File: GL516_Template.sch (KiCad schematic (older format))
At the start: 259 parts, among them J1 Conn_01x02, J10 Conn_01x01, J11 Conn_01x01, J12 Conn_01x01, J13 Conn_01x01, J14 Conn_01x01, J15 Conn_01x01, J16 Conn_01x01, J17 Conn_01x01, J2 Conn_01x01, J3 Conn_01x01, J4 Conn_01x01, J5 Conn_01x01, J6 Conn_01x01, J7 Conn_01x01, J8 Conn_01x01, J9 Conn_01x01, SW1 SW_PUSH, SW10 SW_PUSH, SW11 SW_PUSH, SW12 SW_PUSH, SW13 SW_PUSH, SW14 SW_PUSH, SW15 SW_PUSH, SW16 SW_PUSH, SW17 SW_PUSH, SW18 SW_PUSH, SW19 SW_PUSH, SW2 SW_PUSH, SW20 SW_PUSH, SW21 SW_PUSH, SW22 SW_PUSH, SW23 SW_PUSH, SW24 SW_PUSH, SW25 SW_PUSH, SW26 SW_PUSH, SW27 SW_PUSH, SW28 SW_PUSH, SW29 SW_PUSH, SW3 SW_PUSH, SW30 SW_PUSH, SW31 SW_PUSH, SW32 SW_PUSH, SW33 SW_PUSH, SW34 SW_PUSH, SW35 SW_PUSH, SW36 SW_PUSH, SW37 SW_PUSH, SW38 SW_PUSH, SW39 SW_PUSH, SW4 SW_PUSH, SW40 SW_PUSH, SW41 SW_PUSH, SW42 SW_PUSH, SW43 SW_PUSH, SW44 SW_PUSH, SW45 SW_PUSH, SW46 SW_PUSH, SW47 SW_PUSH, SW48 SW_PUSH, SW49 SW_PUSH, SW5 SW_PUSH, SW50 SW_PUSH, SW51 SW_PUSH, SW52 SW_PUSH, SW53 SW_PUSH, SW54 SW_PUSH, SW55 SW_PUSH, SW56 SW_PUSH, SW57 SW_PUSH, SW58 SW_PUSH, SW59 SW_PUSH, SW6 SW_PUSH, SW60 SW_PUSH, SW61 SW_PUSH, SW62 SW_PUSH, SW63 SW_PUSH, SW64 SW_PUSH, SW65 SW_PUSH, SW66 SW_PUSH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

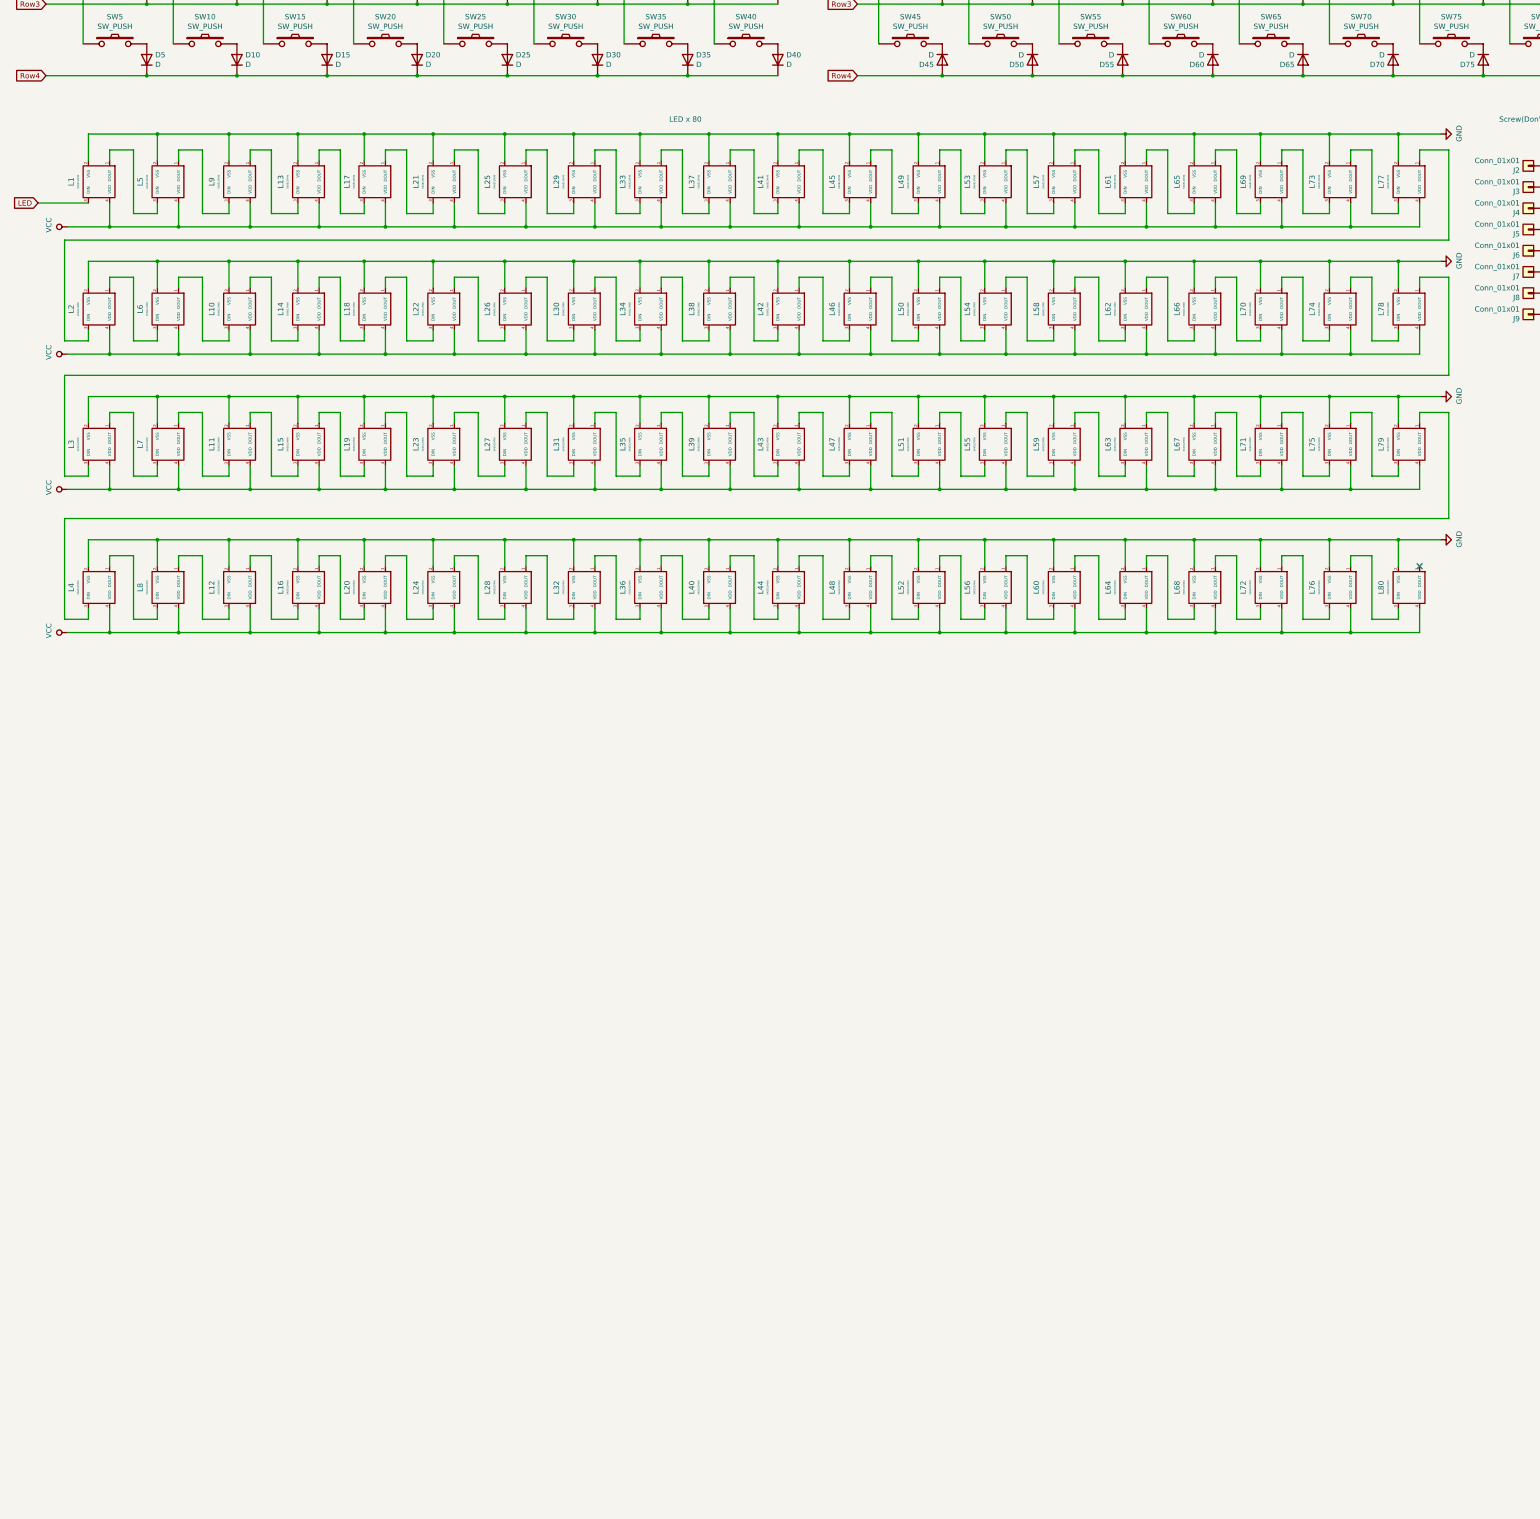
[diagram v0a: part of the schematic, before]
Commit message: LED回路図更新
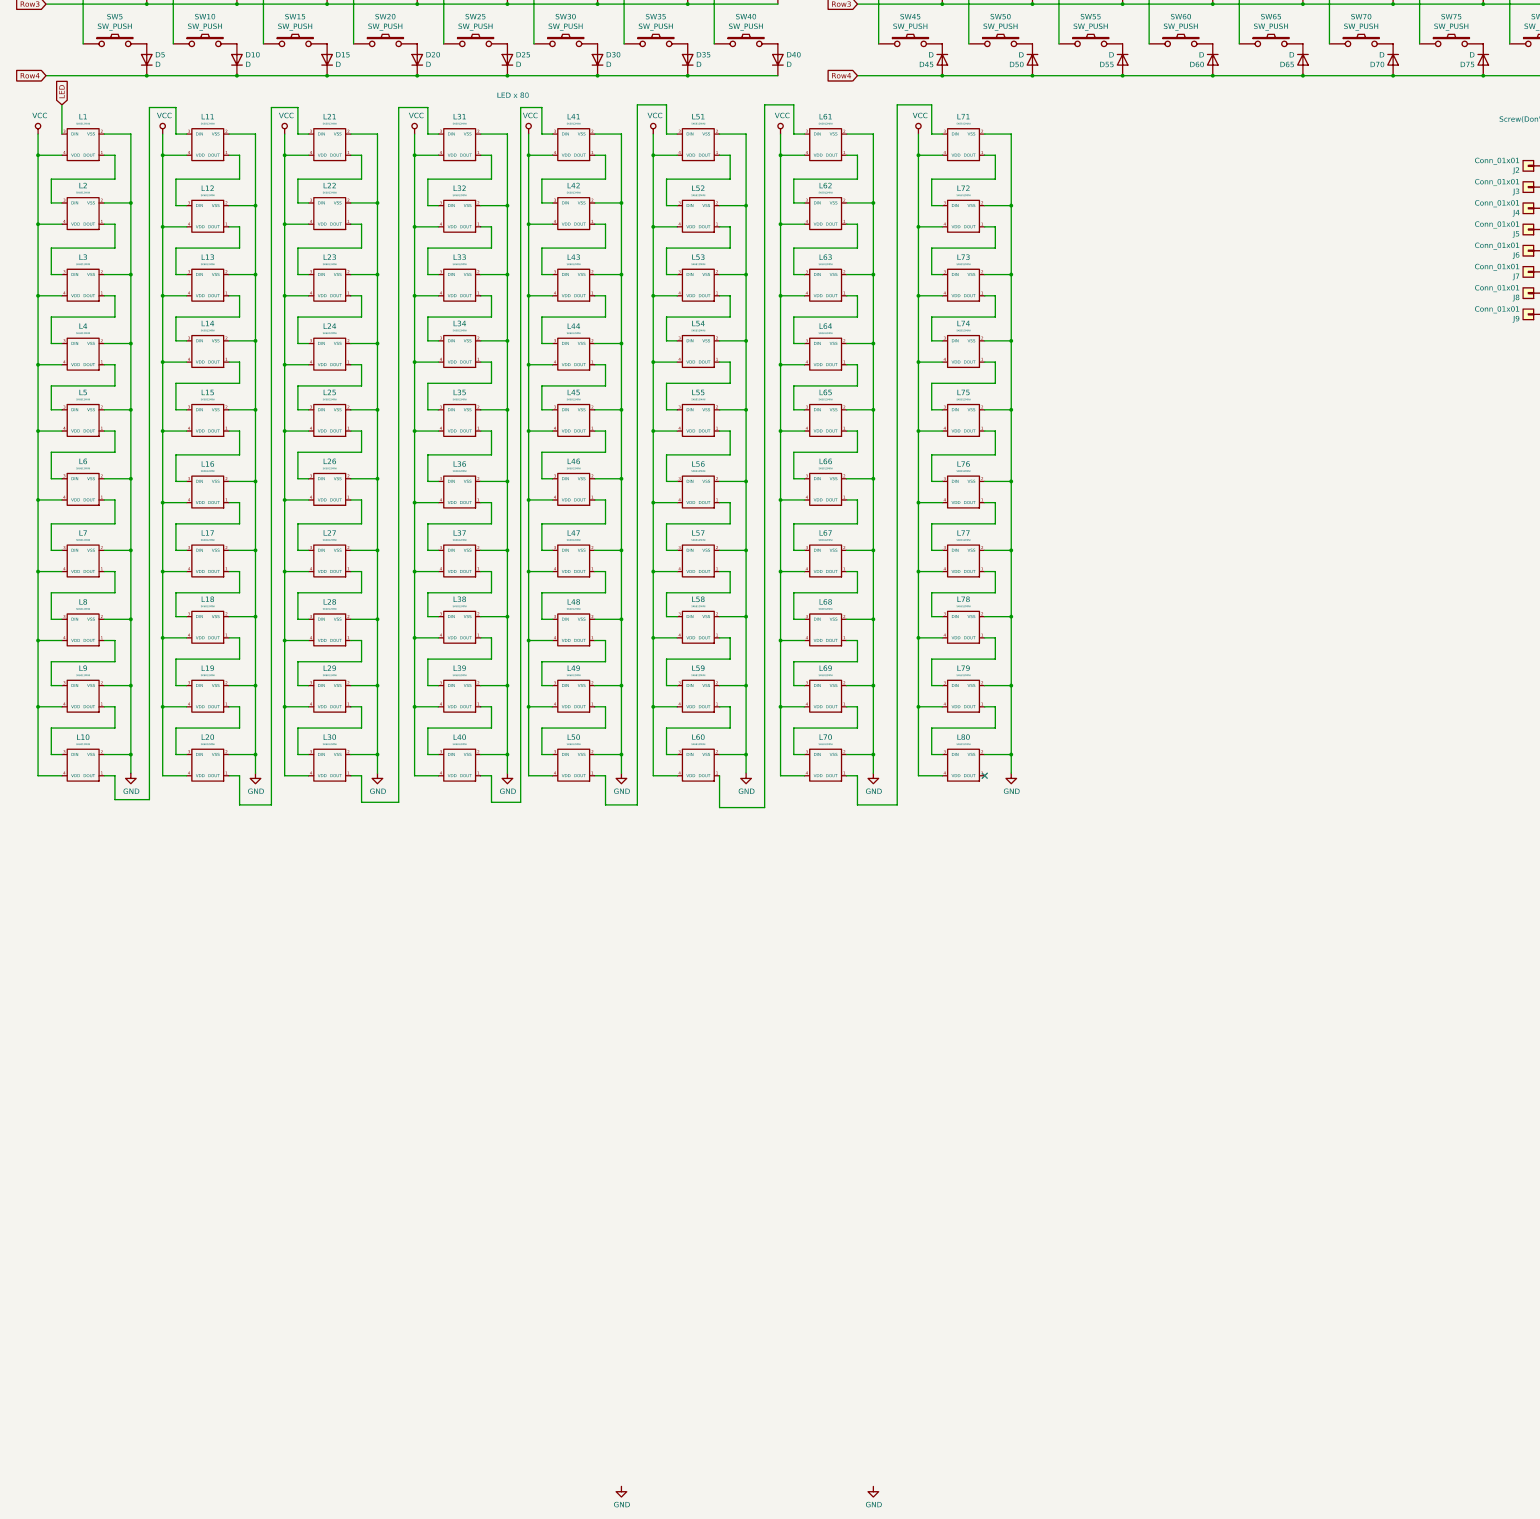
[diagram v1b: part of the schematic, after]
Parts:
- renumbered L37 to L10, L41 to L11, L45 to L12, L49 to L13, L53 to L14, L57 to L15, L61 to L16, L65 to L17, L69 to L18, L73 to L19, L5 to L2, L77 to L20, L2 to L21, L6 to L22, L10 to L23, L14 to L24, L18 to L25, L22 to L26, L26 to L27, L30 to L28, L34 to L29, L9 to L3, L38 to L30, L42 to L31, L46 to L32, L50 to L33, L54 to L34, L58 to L35, L62 to L36, L66 to L37, L70 to L38, L74 to L39, L13 to L4, L78 to L40, L4 to L41, L8 to L42, L12 to L43, L16 to L44, L20 to L45, L24 to L46, L28 to L47, L32 to L48, L36 to L49, L17 to L5, L40 to L50, L44 to L51, L48 to L52, L52 to L53, L56 to L54, L60 to L55, L64 to L56, L68 to L57, L72 to L58, L76 to L59, L21 to L6, L80 to L60, L3 to L61, L7 to L62, L11 to L63, L15 to L64, L19 to L65, L23 to L66, L27 to L67, L31 to L68, L35 to L69, L25 to L7, L39 to L70, L43 to L71, L47 to L72, L51 to L73, L55 to L74, L59 to L75, L63 to L76, L67 to L77, L71 to L78, L75 to L79, L29 to L8, L79 to L80, L33 to L9
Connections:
- net at L61.3 (DIN): now also L60.1 (DOUT); no longer L40.1 (DOUT)
- net at L41.3 (DIN): now also L40.1 (DOUT); no longer L80.1 (DOUT)
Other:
- moved on the sheet: L1, L10, L11, L12, L13, L14, L15, L16, L17, L18, L19, L2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

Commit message: フットプリントを更新
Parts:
- D1, D10, D11, D12, D13, D14, D15, D16, D17, D18, D19, D2, D20, D21, D22, D23, D24, D25, D26, D27, D28, D29, D3, D30, D31, D32, D33, D34, D35, D36, D37, D38, D39, D4, D40, D41, D42, D43, D44, D45, D46, D47, D48, D49, D5, D50, D51, D52, D53, D54, D55, D56, D57, D58, D59, D6, D60, D61, D62, D63, D64, D65, D66, D67, D68, D69, D7, D70, D71, D72, D73, D74, D75, D76, D77, D78, D79, D8, D80, D9: footprint kbd:D3_TH_SMD_BL -> kbd_Parts:Diode_TH_SMD
- J1: footprint kbd:XH2.5_rev -> kbd_Parts:Battery_XH2.5_GL
- J10, J11, J12, J13, J14, J15, J16, J17, J8, J9: footprint kbd:HOLE_m2_Outline_Fab -> kbd_Hole:m2_Screw_Hole_Fab
- J2, J3, J4, J5, J6, J7: footprint kbd:HOLE_m2_Outline -> kbd_Hole:m2_Screw_Hole_EdgeCuts
- L1, L10, L11, L12, L13, L14, L15, L16, L17, L18, L19, L2, L20, L21, L22, L23, L24, L25, L26, L27, L28, L29, L3, L30, L31, L32, L33, L34, L35, L36, L37, L38, L39, L4, L40, L41, L42, L43, L44, L45, L46, L47, L48, L49, L5, L50, L51, L52, L53, L54, L55, L56, L57, L58, L59, L6, L60, L61, L62, L63, L64, L65, L66, L67, L68, L69, L7, L70, L71, L72, L73, L74, L75, L76, L77, L78, L79, L8, L80, L9: footprint kbd:YS-SK6812MINI-E_v3 -> kbd_Parts:LED_SK6812MINI-E_BL
- SW1, SW10, SW11, SW12, SW13, SW14, SW15, SW16, SW17, SW18, SW19, SW2, SW20, SW21, SW22, SW23, SW24, SW25, SW26, SW27, SW28, SW29, SW3, SW30, SW31, SW32, SW33, SW34, SW35, SW36, SW37, SW38, SW39, SW4, SW40, SW41, SW42, SW43, SW44, SW45, SW46, SW47, SW48, SW49, SW5, SW50, SW51, SW52, SW53, SW54, SW55, SW56, SW57, SW58, SW59, SW6, SW60, SW61, SW62, SW63, SW64, SW65, SW66, SW67, SW68, SW69, SW7, SW70, SW71, SW72, SW73, SW74, SW75, SW76, SW77, SW78, SW79, SW8, SW80, SW9: footprint kbd:CherryMX_Choc_Hotswap_LH_v2 -> kbd_SW:CherryMX_Choc_Hotswap_1u
- SW81: footprint kbd:ResetSW -> kbd_Parts:ResetSW
- U1: footprint kbd:BLE_Micro_Pro_L1 -> kbd_Parts:Micon_BMP_GL
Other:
- note added: "Left hand block (Max 40 keys)"
- note added: "Right hand block (Max 40 keys)"
- note removed: "Left hand block (Max 35 keys)"
- note removed: "Right hand block (Max 35 keys)"
